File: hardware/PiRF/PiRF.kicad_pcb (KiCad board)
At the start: 4 copper layers, 65 x 56 mm, 52 parts, among them J1 Conn_02x20_Counter_Clockwise, J3 40HAT, J6 CONN_02X02, J9 CONN_01X02, Q1 DMG2305UX, Q2 DMMT5401, U1 TPS7A19, U2 CAT24C32

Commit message: Updated the design. Ready to start layout.
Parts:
- removed J6: CONN_02X02, Connector_PinHeader_2.54mm:PinHeader_2x02_P2.54mm_Vertical
- removed Q1: DMG2305UX, Package_TO_SOT_SMD:SOT-23
- removed Q2: DMMT5401, Package_TO_SOT_SMD:SOT-23-6
- removed R23: 10K, Resistor_SMD:R_0603_1608Metric_Pad0.84x1.00mm_HandSolder
- removed R24: 47K, Resistor_SMD:R_0603_1608Metric_Pad0.84x1.00mm_HandSolder
- removed TP10, TP12, TP13, TP16, TP17, TP18, TP19, TP20, TP21, TP22, TP23, TP24, TP5, TP6, TP7, TP8, TP9: TestPoint, TestPoint:TestPoint_Pad_D1.0mm
- added D1: LED, LED_SMD:LED_0603_1608Metric_Pad1.05x0.95mm_HandSolder, F.Cu at (86.5, 111.5)
- added D2: LED, LED_SMD:LED_0603_1608Metric_Pad1.05x0.95mm_HandSolder, F.Cu at (90.0, 111.5)
- added D3: LED, LED_SMD:LED_0603_1608Metric_Pad1.05x0.95mm_HandSolder, F.Cu at (94.0, 111.5)
- added D4: LED, LED_SMD:LED_0603_1608Metric_Pad1.05x0.95mm_HandSolder, F.Cu at (98.5, 111.5)
- added DWM1: DWM1000, RF_Module:DWM1000, F.Cu at (81.0, 94.0)
- added H5: 3mm_Mounting_Hole, MountingHole:MountingHole_2.1mm, F.Cu at (104.0, 81.0)
- added H6: 3mm_Mounting_Hole, MountingHole:MountingHole_2.1mm, F.Cu at (104.0, 106.0)
- added H7: 3mm_Mounting_Hole, MountingHole:MountingHole_2.1mm, F.Cu at (140.0, 81.0)
- added H8: 3mm_Mounting_Hole, MountingHole:MountingHole_2.1mm, F.Cu at (140.0, 106.0)
- added R10: DNP, Resistor_SMD:R_0603_1608Metric_Pad1.05x0.95mm_HandSolder, F.Cu at (100.0, 93.5)
- added R12: 0, Resistor_SMD:R_0603_1608Metric_Pad1.05x0.95mm_HandSolder, F.Cu at (100.0, 95.5)
- added R13: 1.5k, Resistor_SMD:R_0603_1608Metric_Pad1.05x0.95mm_HandSolder, F.Cu at (94.0, 106.0)
- added R14: 1.5k, Resistor_SMD:R_0603_1608Metric_Pad1.05x0.95mm_HandSolder, F.Cu at (98.5, 106.0)
- added R4: 1.5k, Resistor_SMD:R_0603_1608Metric_Pad1.05x0.95mm_HandSolder, F.Cu at (86.5, 106.0)
- added R5: DNP, Resistor_SMD:R_0603_1608Metric_Pad1.05x0.95mm_HandSolder, F.Cu at (100.0, 97.5)
- R7: value DNP -> 0; footprint Resistor_SMD:R_0603_1608Metric_Pad0.84x1.00mm_HandSolder -> Resistor_SMD:R_0603_1608Metric_Pad1.05x0.95mm_HandSolder
- R9: value DNP -> 1.5k; footprint Resistor_SMD:R_0603_1608Metric_Pad0.84x1.00mm_HandSolder -> Resistor_SMD:R_0603_1608Metric_Pad1.05x0.95mm_HandSolder
- moved TP3 60.3 mm to (136.0, 74.0), turned to 180 degrees
- moved TP25 47.9 mm to (140.0, 74.0), turned to 180 degrees
- moved TP14 43.9 mm to (133.0, 72.0), turned to 180 degrees
- moved TP1 43.1 mm to (138.0, 71.5), turned to 180 degrees
- moved TP2 40.3 mm to (136.0, 110.0)
- moved TP11 38.8 mm to (131.0, 75.0), turned to 180 degrees
- moved R9 37.7 mm to (90.0, 106.0), turned to 90 degrees
- moved J1 35.2 mm to (133.0, 93.5), turned to 180 degrees
- moved TP4 31.2 mm to (132.5, 112.5)
- moved R1 28.5 mm to (108.5, 85.5), turned to 0 degrees
- moved C1 27.5 mm to (113.1, 85.5), turned to 0 degrees
- moved R7 24.1 mm to (100.0, 99.5)
- moved C2 22.5 mm to (109.0, 95.0), turned to 180 degrees
- moved TP15 21.1 mm to (129.0, 112.5)
- moved U1 20.4 mm to (113.1, 90.2), turned to 90 degrees
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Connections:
- J1 pad 21: /SCLK -> Net-(J1-Pad21)
- J1 pad 23: /MOSI -> Net-(J1-Pad23)
- J1 pad 25: /MISO -> Net-(J1-Pad25)
- J1 pad 27: /SS -> Net-(J1-Pad27)
- J3 pad 31: Net-(J3-Pad31) -> /UWB_RSTn
- R7 pad 1: /P3V3_HAT -> Net-(DWM1-Pad9)
- R7 pad 2: /P3V3 -> GND
- R9 pad 1: /P5V_HAT -> Net-(D2-Pad1)
- R9 pad 2: /P5V -> Net-(DWM1-Pad14)
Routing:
- net /P3V3: track 31.3 -> 0.00 mm
- net /P5V: track 8.71 -> 0.00 mm
- net Net-(Q1-Pad1): track 6.02 -> 0.00 mm
- net /P5V_HAT: track 3.77 -> 0.00 mm
- net Net-(Q2-Pad1): track 3.37 -> 0.00 mm
- net /P3V3_HAT: track 2.88 -> 0.00 mm
- removed copper zone on F.Cu, net /P5V
- removed copper zone on B.Cu, net /P5V_HAT
- removed copper zone on F.Cu, net /P5V_HAT
- removed copper zone on B.Cu, net Net-(J3-Pad1)

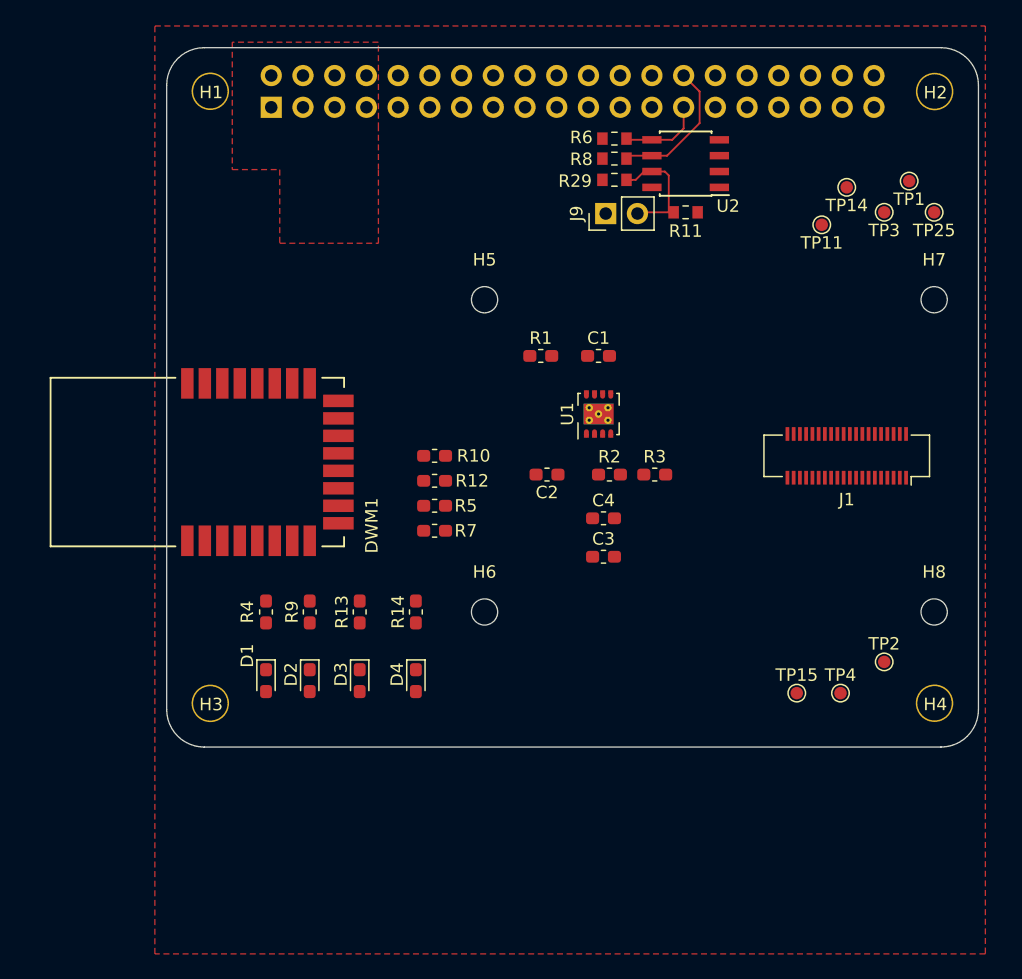
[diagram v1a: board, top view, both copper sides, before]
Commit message: Updated and started to route signals.
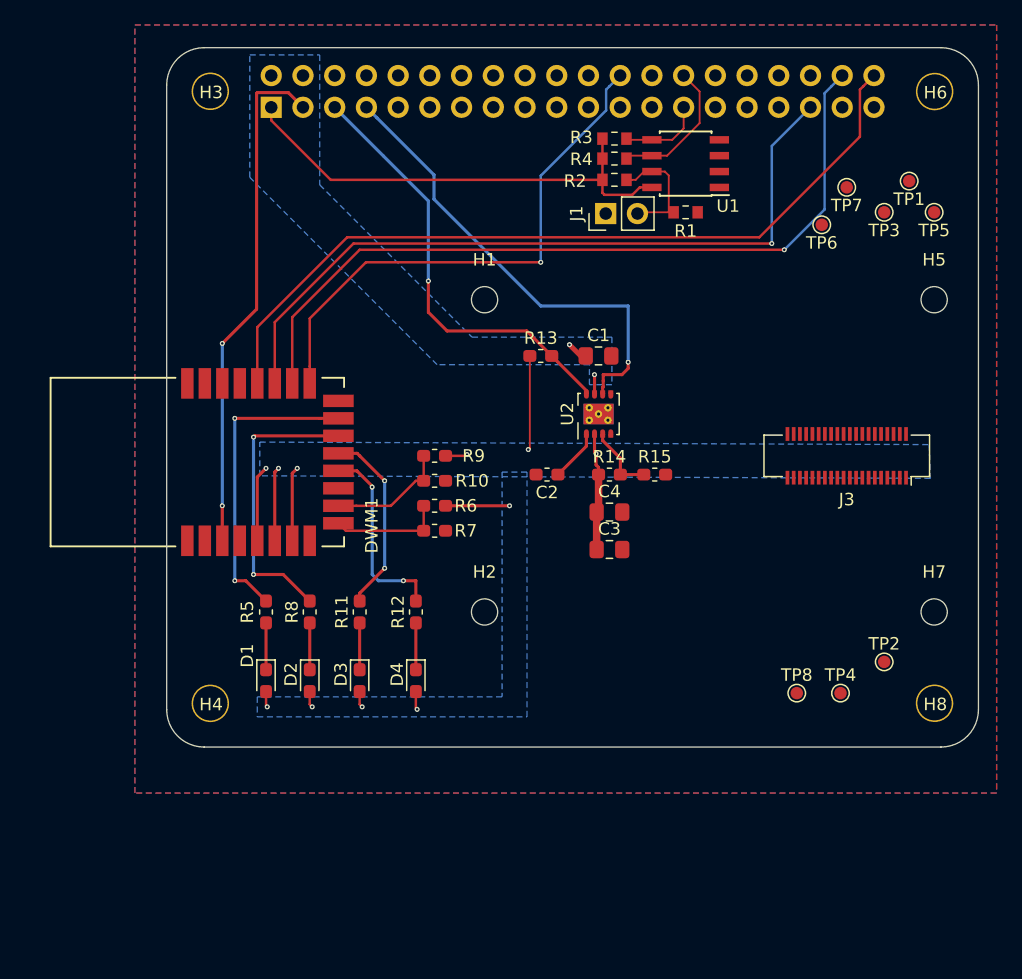
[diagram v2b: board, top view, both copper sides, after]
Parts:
- C1, C3, C4: footprint Capacitor_SMD:C_0603_1608Metric_Pad1.05x0.95mm_HandSolder -> Capacitor_SMD:C_0805_2012Metric_Pad1.15x1.40mm_HandSolder
- moved C3 0.75 mm to (114.0, 101.0)
- moved C4 0.69 mm to (114.0, 98.0)
- renumbered H5 to H1, H6 to H2, H1 to H3, H3 to H4, H7 to H5, H2 to H6, H8 to H7, H4 to H8, J9 to J1, J3 to J2, J1 to J3, R11 to R1, R12 to R10, R13 to R11, R14 to R12, R1 to R13, R2 to R14, R3 to R15, R29 to R2, R6 to R3, R8 to R4, R4 to R5, R5 to R6, R9 to R8, R10 to R9, TP25 to TP5, TP11 to TP6, TP14 to TP7, TP15 to TP8, U2 to U1, U1 to U2
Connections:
- J2 pad 1: Net-(J3-Pad1) -> /HAT_3V3
- J2 pad 21: /HAT_PWR_EN -> Net-(J2-Pad21)
- J2 pad 23: /HAT_PG -> Net-(J2-Pad23)
- J2 pad 3: Net-(J3-Pad3) -> /UWB_RSTn
- J2 pad 31: /UWB_RSTn -> Net-(J2-Pad31)
- J2 pad 5: Net-(J3-Pad5) -> /HAT_PG
- J2 pad 7: Net-(J3-Pad7) -> /HAT_PWR_EN
- R2 pad 1: /P3V3 -> /HAT_3V3
- R3 pad 1: /P3V3 -> /HAT_3V3
- R4 pad 1: /P3V3 -> /HAT_3V3
- U1 pad 8: +3V3 -> /HAT_3V3
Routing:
- net /SCLK: track 0.00 -> 64.4 mm
- net /MOSI: track 0.00 -> 62.8 mm, vias 0 -> 1
- net /MISO: track 0.00 -> 59.5 mm, vias 0 -> 1
- net +3V3: track 0.00 -> 47.3 mm, vias 0 -> 11
- net /SS: track 0.00 -> 43.1 mm, vias 0 -> 1
- net /UWB_RSTn: track 0.00 -> 41.2 mm, vias 0 -> 2
- net /HAT_3V3: track 0.00 -> 38.2 mm
- net /HAT_PWR_EN: track 0.00 -> 37.5 mm, vias 0 -> 1
- net /HAT_PG: track 0.00 -> 35.1 mm, vias 0 -> 1
- net Net-(DWM1-Pad15): track 0.00 -> 24.5 mm, vias 0 -> 2
- net Net-(DWM1-Pad14): track 0.00 -> 23.2 mm, vias 0 -> 2
- net Net-(DWM1-Pad12): track 0.00 -> 15.6 mm, vias 0 -> 2
- net Net-(DWM1-Pad13): track 0.00 -> 15.1 mm, vias 0 -> 2
- net Net-(DWM1-Pad10): track 0.00 -> 9.66 mm
- net Net-(DWM1-Pad9): track 0.00 -> 9.08 mm
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- added copper zone on B.Cu, net +3V3
- added copper zone on B.Cu, net /P5V_HAT
- added copper zone on B.Cu, net GND
- removed copper zone on In2.Cu, net GND
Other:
- copper layers 4 -> 2

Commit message: Finished layout
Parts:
- removed TP7, TP8: TestPoint, TestPoint:TestPoint_Pad_D1.0mm
- added J4: CONN_01X02, Connector_PinHeader_2.54mm:PinHeader_1x02_P2.54mm_Vertical, F.Cu at (136.5, 74.0)
- J3: value Conn_02x20_Counter_Clockwise -> Conn_02x20_Odd_Even
- moved TP5 49.9 mm to (109.5, 113.5)
- moved TP1 43.5 mm to (128.5, 114.0)
- moved TP3 39.7 mm to (120.5, 110.5)
- moved TP4 15.6 mm to (117.0, 114.0)
- moved TP2 10.0 mm to (126.0, 110.5)
- moved TP6 9.50 mm to (140.5, 75.0)
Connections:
- DWM1 pad 1: Net-(DWM1-Pad1) -> (no net)
- DWM1 pad 11: Net-(DWM1-Pad11) -> (no net)
- DWM1 pad 22: /UWB_IRQ -> (no net)
- DWM1 pad 4: Net-(DWM1-Pad4) -> (no net)
- J2 pad 11: /BL_ENABLE -> (no net)
- J2 pad 12: Net-(J2-Pad12) -> (no net)
- J2 pad 13: /RESET_N -> (no net)
- J2 pad 15: /GPIO0 -> (no net)
- J2 pad 16: Net-(J2-Pad16) -> (no net)
- J2 pad 17: Net-(J2-Pad17) -> (no net)
- J2 pad 18: Net-(J2-Pad18) -> (no net)
- J2 pad 19: /GPIO1 -> (no net)
- J2 pad 21: Net-(J2-Pad21) -> (no net)
- J2 pad 22: Net-(J2-Pad22) -> (no net)
- J2 pad 23: Net-(J2-Pad23) -> (no net)
- J2 pad 26: Net-(J2-Pad26) -> (no net)
- J2 pad 31: Net-(J2-Pad31) -> (no net)
- J2 pad 32: Net-(J2-Pad32) -> /BL_ENABLE
- J2 pad 33: Net-(J2-Pad33) -> /GPIO0
- J2 pad 36: Net-(J2-Pad36) -> /GPIO1
- J2 pad 37: Net-(J2-Pad37) -> /RESET_N
- J3 pad 10: GND -> /UART_RXD
- J3 pad 11: Net-(J3-Pad11) -> /GPIO1
- J3 pad 12: Net-(J3-Pad12) -> /UART_TXD
- J3 pad 13: GND -> /BL_ENABLE
- J3 pad 14: Net-(J3-Pad14) -> GND
- J3 pad 15: GND -> /GPIO0
- J3 pad 16: Net-(J3-Pad16) -> (no net)
- J3 pad 17: GND -> /WAKEUP
- J3 pad 18: Net-(J3-Pad18) -> (no net)
- J3 pad 2: +3V3 -> /RESET_N
- J3 pad 20: Net-(J3-Pad20) -> (no net)
- J3 pad 21: Net-(J3-Pad21) -> (no net)
- J3 pad 22: GND -> (no net)
- J3 pad 23: Net-(J3-Pad23) -> (no net)
- J3 pad 25: Net-(J3-Pad25) -> GND
- J3 pad 26: GND -> (no net)
- J3 pad 27: Net-(J3-Pad27) -> (no net)
- J3 pad 28: Net-(J3-Pad28) -> (no net)
- J3 pad 30: Net-(J3-Pad30) -> GND
- J3 pad 31: Net-(J3-Pad31) -> (no net)
- J3 pad 32: Net-(J3-Pad32) -> (no net)
- J3 pad 33: Net-(J3-Pad33) -> GND
- J3 pad 35: /UART_TXD -> (no net)
- J3 pad 36: /UART_RXD -> (no net)
- J3 pad 38: Net-(J3-Pad38) -> GND
- J3 pad 39: Net-(J3-Pad39) -> (no net)
- J3 pad 4: +3V3 -> (no net)
- J3 pad 40: /RESET_N -> (no net)
- J3 pad 5: GND -> +3V3
- J3 pad 6: /GPIO1 -> (no net)
- J3 pad 7: /BL_ENABLE -> +3V3
- J3 pad 8: /GPIO0 -> GND
- J3 pad 9: /WAKEUP -> GND
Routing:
- net /WAKEUP: track 0.00 -> 111.0 mm, vias 0 -> 4
- net /GPIO0: track 0.00 -> 71.6 mm, vias 0 -> 6
- net /UART_RXD: track 0.00 -> 67.5 mm, vias 0 -> 3
- net /GPIO1: track 0.00 -> 66.0 mm, vias 0 -> 3
- net /UART_TXD: track 0.00 -> 66.0 mm
- net /BL_ENABLE: track 0.00 -> 61.9 mm, vias 0 -> 5
- net /RESET_N: track 0.00 -> 31.7 mm, vias 0 -> 1
- net +3V3: track 47.3 -> 57.7 mm, vias 11 -> 16
- net GND: vias 0 -> 4
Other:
- board text added: "PiRFHat Rev A"
- board text added: "RX"
- board text added: "RXOK"
- board text added: "SFD"
- board text added: "TX"

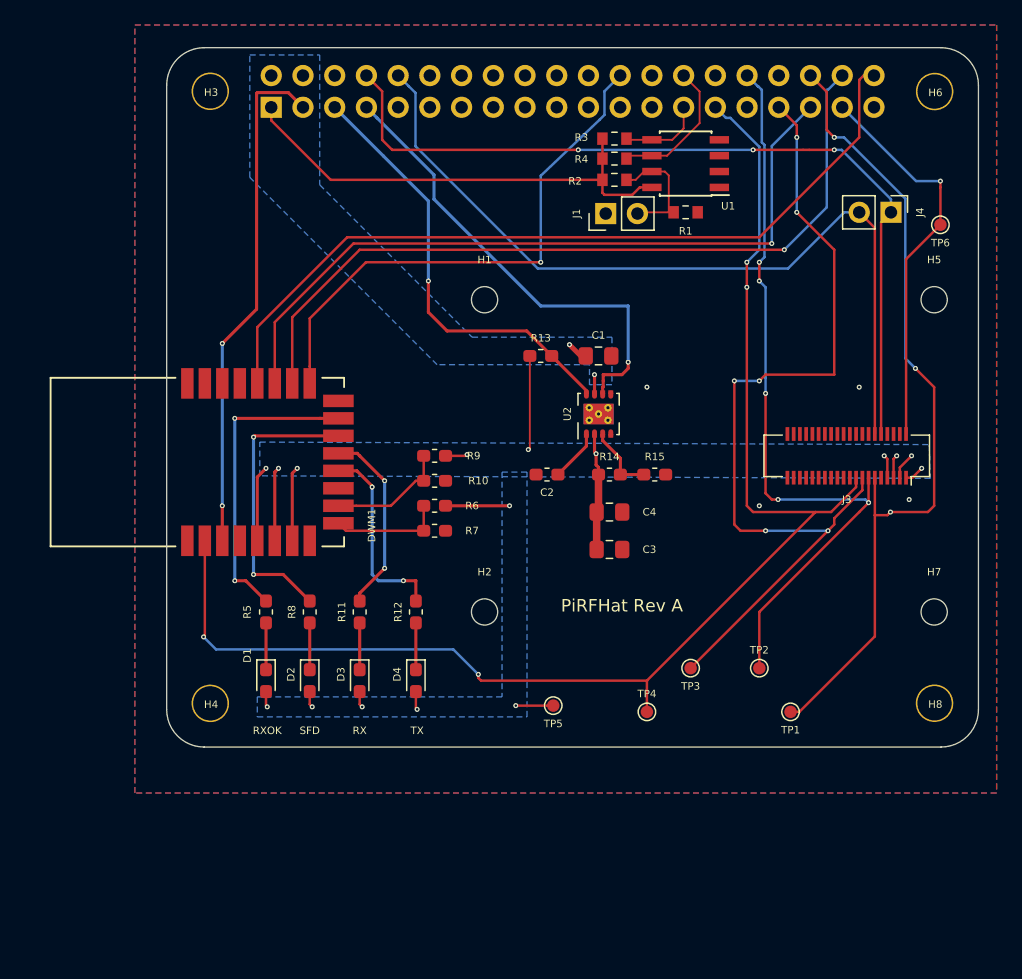
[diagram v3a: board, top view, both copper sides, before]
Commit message: Added GPS to the design, haven't routed the design yet.
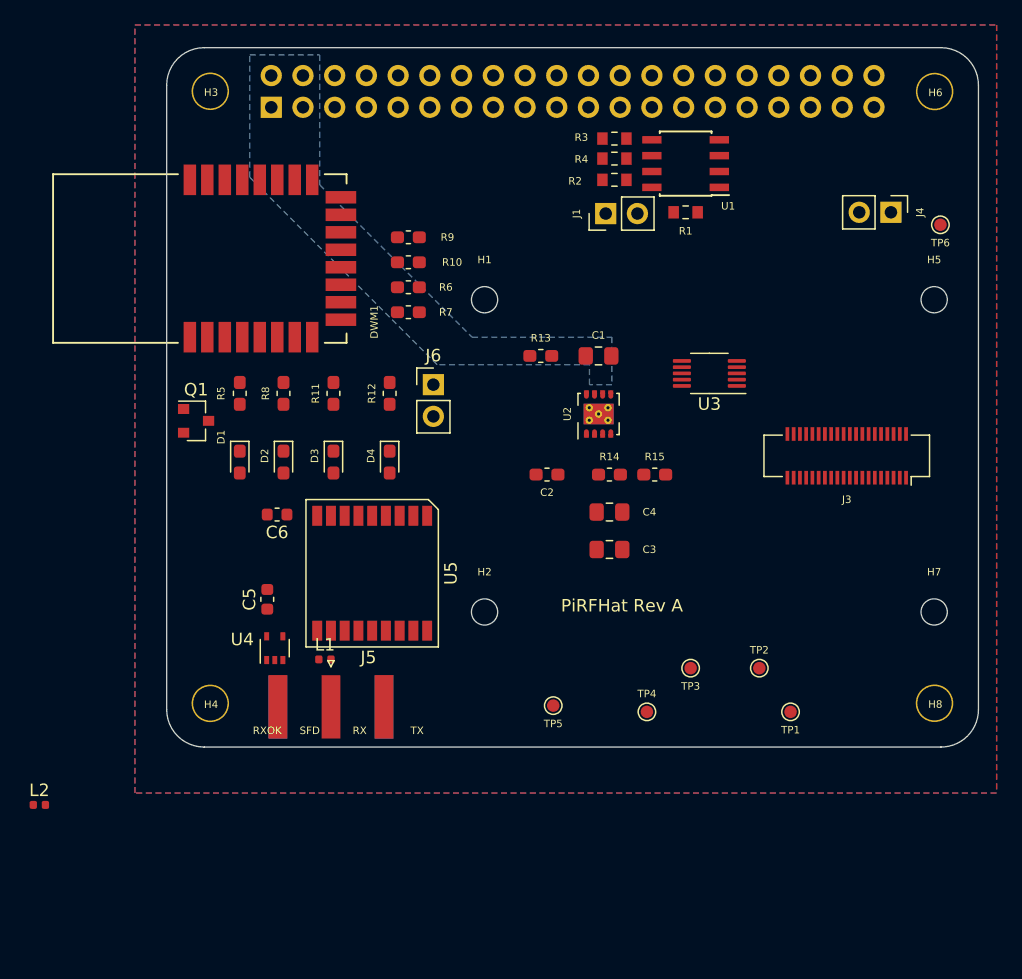
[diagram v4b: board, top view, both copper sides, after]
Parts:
- added C5: 56P, Capacitor_SMD:C_0603_1608Metric, F.Cu at (86.6, 105.0)
- added C6: 56P, Capacitor_SMD:C_0603_1608Metric, F.Cu at (87.4, 98.2)
- added J5: Conn_Coaxial, Connector_Coaxial:SMA_Amphenol_132289_EdgeMount, F.Cu at (91.7, 113.6)
- added J6: CONN_01X02, Connector_PinHeader_2.54mm:PinHeader_1x02_P2.54mm_Vertical, F.Cu at (99.9, 87.8)
- added L1: 27n, Inductor_SMD:L_0402_1005Metric, F.Cu at (91.2, 109.8)
- added L2: 27n, Inductor_SMD:L_0402_1005Metric, F.Cu at (68.3, 121.5)
- added Q1: MMBT3904, Package_TO_SOT_SMD:SOT-23, F.Cu at (80.9, 90.7)
- added U3: TS5A23159, Package_SO:VSSOP-10_3x3mm_P0.5mm, F.Cu at (122.0, 86.9)
- added U4: TPS2294x, Package_TO_SOT_SMD:SOT-353_SC-70-5, F.Cu at (87.2, 108.9)
- added U5: ST_Teseo, KicadFootprint:TESEO-LIV3R, F.Cu at (95.0, 102.9)
- moved D1 17.6 mm to (84.4, 94.0)
- moved D2 17.6 mm to (87.9, 94.0)
- moved D3 17.6 mm to (91.9, 94.0)
- moved D4 17.6 mm to (96.4, 94.0)
- moved R10 17.6 mm to (97.9, 78.0)
- moved R11 17.6 mm to (91.9, 88.5)
- moved R12 17.6 mm to (96.4, 88.5)
- moved R5 17.6 mm to (84.4, 88.5)
- moved R6 17.6 mm to (97.9, 80.0)
- moved R7 17.6 mm to (97.9, 82.0)
- moved R8 17.6 mm to (87.9, 88.5)
- moved R9 17.6 mm to (97.9, 76.0)
- moved DWM1 16.3 mm to (81.2, 77.7)
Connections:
- DWM1 pad 3: /UWB_RSTn -> Net-(DWM1-Pad3)
- J2 pad 11: (no net) -> /HAT_PG
- J2 pad 13: (no net) -> /HAT_PWR_EN
- J2 pad 15: (no net) -> /GPS_PPS
- J2 pad 17: (no net) -> /GPS_RESETn
- J2 pad 19: (no net) -> /GPS_WAKE
- J2 pad 21: (no net) -> /UART_MUX
- J2 pad 23: (no net) -> /GPS_ANT_OC
- J2 pad 3: /UWB_RSTn -> /GPS_SDA
- J2 pad 5: /HAT_PG -> /GPS_SCL
- J2 pad 7: /HAT_PWR_EN -> /UWB_RSTn
- J3 pad 10: /UART_RXD -> /GRIM_RXD
- J3 pad 12: /UART_TXD -> /GRIM_TXD
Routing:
- net /WAKEUP: track 111.0 -> 0.00 mm, vias 4 -> 0
- net /GPIO0: track 71.6 -> 0.00 mm, vias 6 -> 0
- net /UART_RXD: track 67.5 -> 0.00 mm, vias 3 -> 0
- net /GPIO1: track 66.0 -> 0.00 mm, vias 3 -> 0
- net /UART_TXD: track 66.0 -> 0.00 mm
- net /SCLK: track 64.9 -> 0.00 mm
- net /MOSI: track 62.9 -> 0.00 mm, vias 1 -> 0
- net /BL_ENABLE: track 61.9 -> 0.00 mm, vias 5 -> 0
- net /MISO: track 59.5 -> 0.00 mm, vias 1 -> 0
- net +3V3: track 57.7 -> 0.00 mm, vias 16 -> 0
- net /SS: track 43.2 -> 0.00 mm, vias 1 -> 0
- net /UWB_RSTn: track 41.2 -> 0.00 mm, vias 2 -> 0
- net /HAT_3V3: track 38.2 -> 0.00 mm
- net /HAT_PWR_EN: track 37.5 -> 0.00 mm, vias 1 -> 0
- net /HAT_PG: track 35.1 -> 0.00 mm, vias 1 -> 0
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- removed copper zone on B.Cu, net +3V3
